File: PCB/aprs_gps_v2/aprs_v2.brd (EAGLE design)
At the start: 61 x 61 mm, 17 parts, among them X1 BU-SMA-V

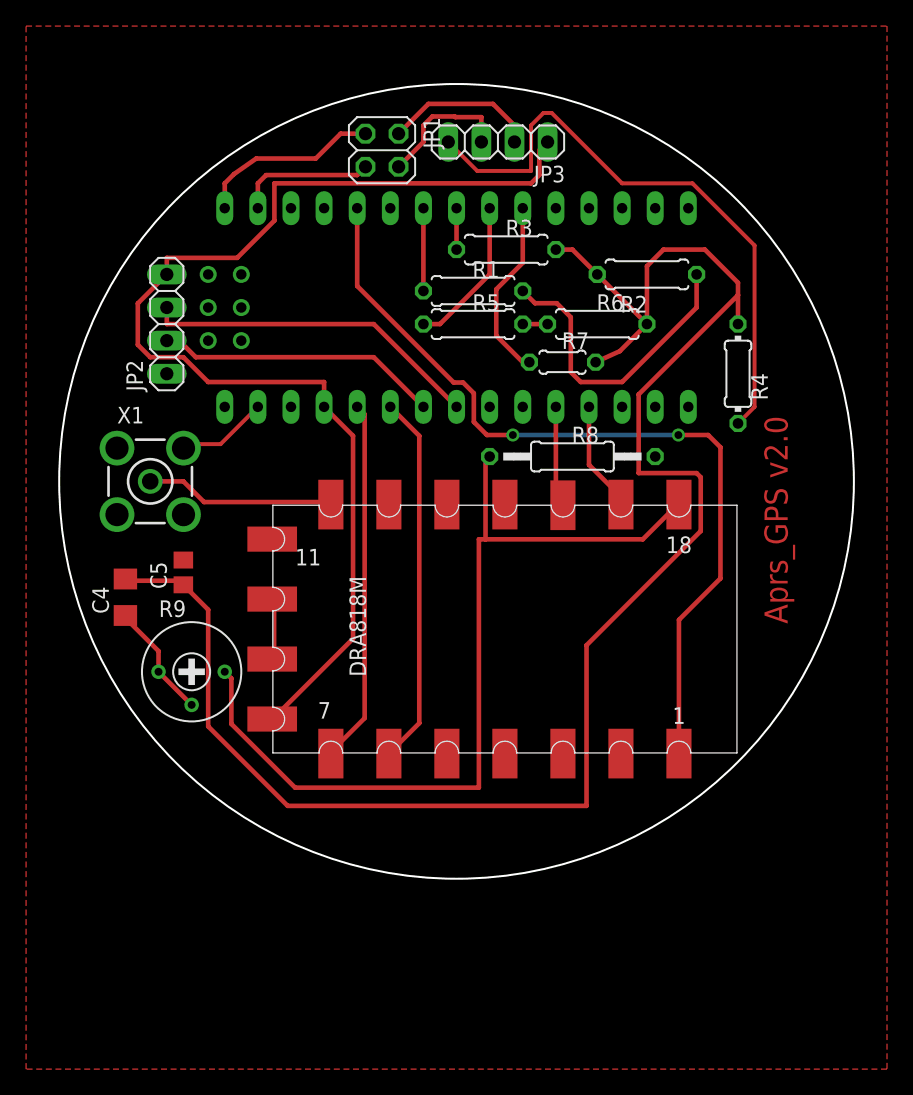
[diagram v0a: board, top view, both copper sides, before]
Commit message: fix VCC and Vin
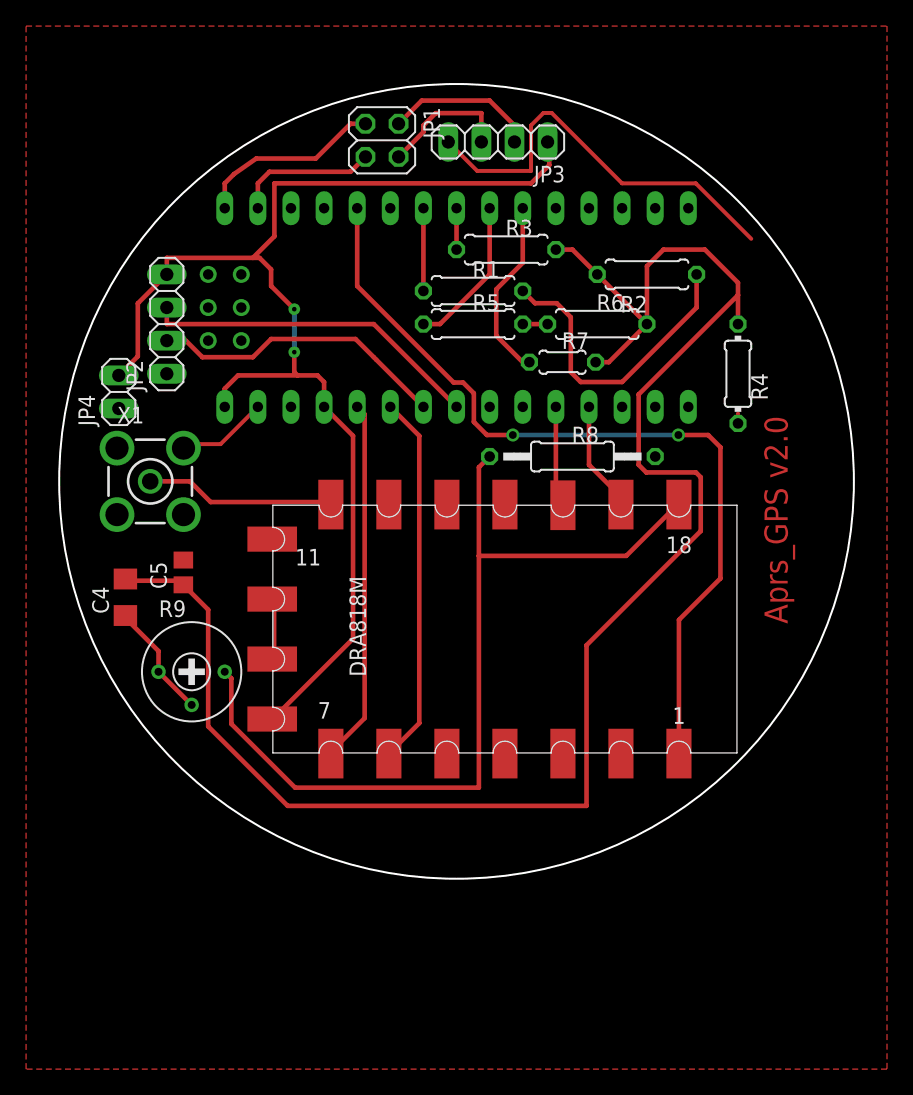
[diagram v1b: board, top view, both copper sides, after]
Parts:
- added JP4: (no value), pinhead:1X02
- moved JP1 0.76 mm to (29.8, 63.0)
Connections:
- net GND: now also JP4.1
- net VCC: now also JP4.2, U$2.RAW
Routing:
- net GND: track 59.0 -> 45.1 mm
- net VCC: track 88.1 -> 97.0 mm, vias 0 -> 2
- net SCL: track 21.8 -> 22.9 mm
- net MC_APRS_OUT: track 67.2 -> 67.9 mm
